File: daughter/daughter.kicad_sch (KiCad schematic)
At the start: 2 parts, among them U1 ESP32-C3, Y1 Crystal_GND24_Small

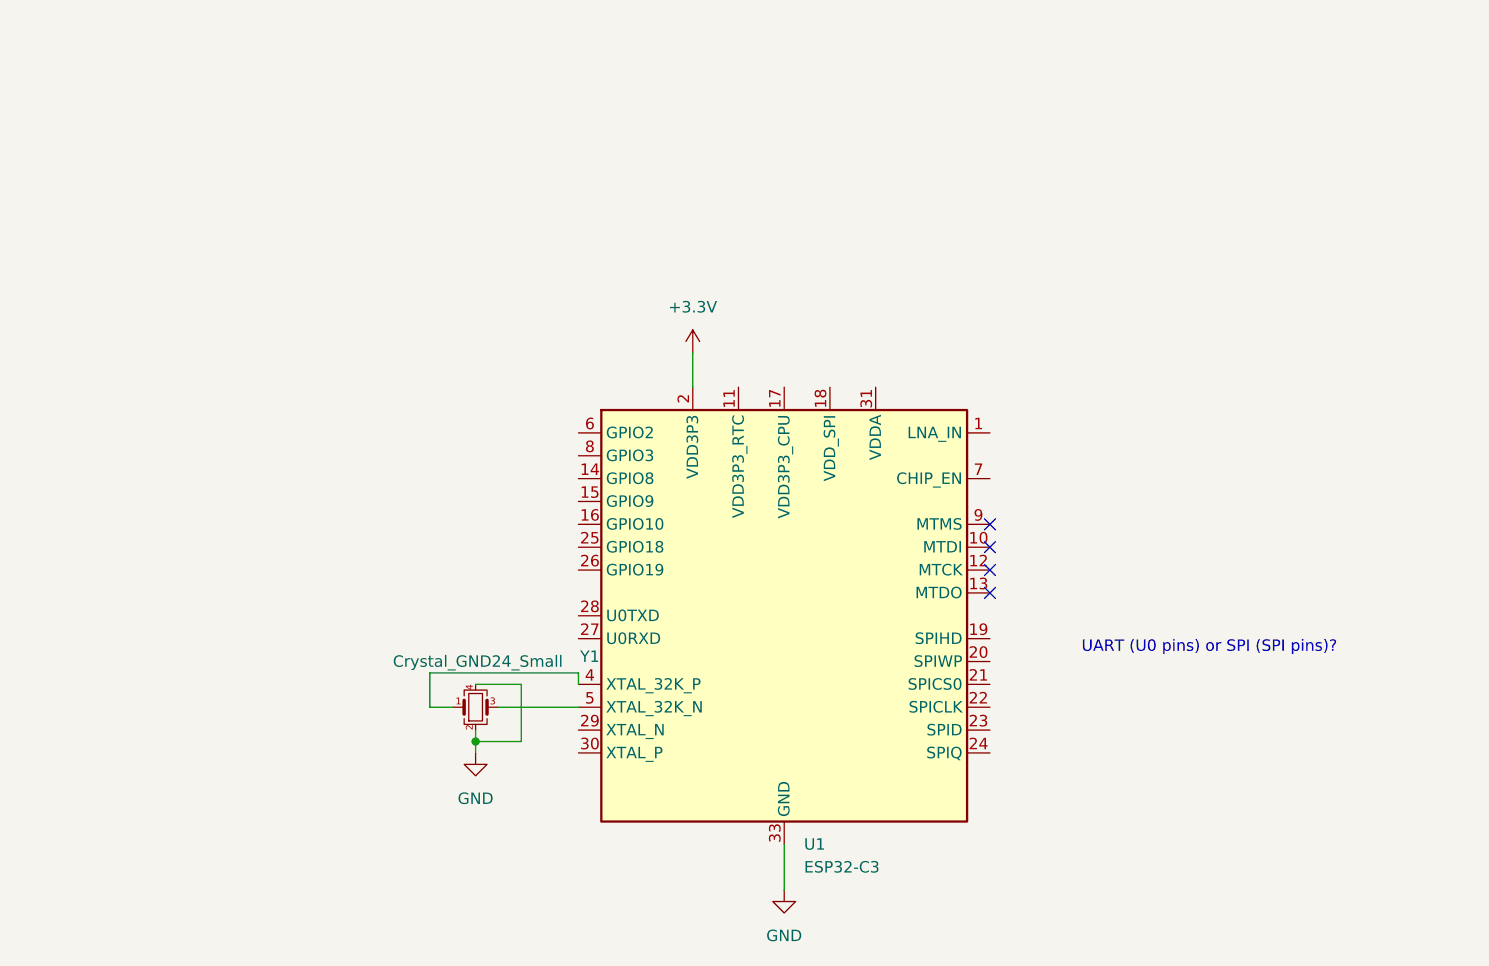
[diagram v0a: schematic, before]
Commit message: Daughterboard setup, labeling, and testpoints
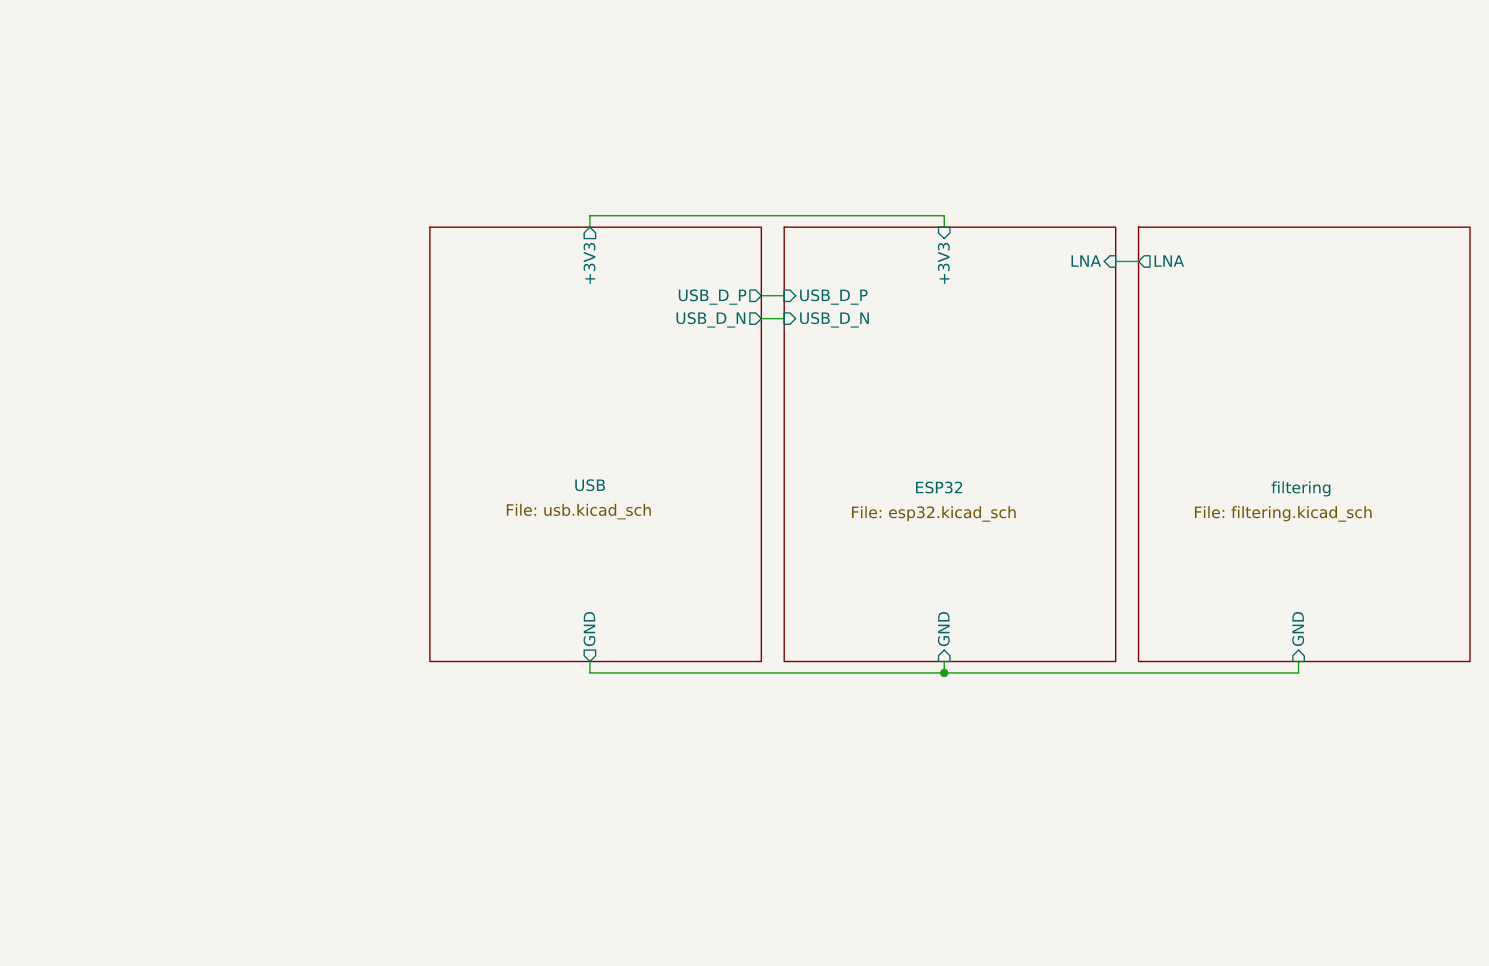
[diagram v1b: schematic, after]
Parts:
- removed U1: ESP32-C3, Package_DFN_QFN:QFN-32-1EP_5x5mm_P0.5mm_EP3.7x3.7mm, symbol MCU_Espressif:ESP32-C3
- removed Y1: Crystal_GND24_Small, symbol Device:Crystal_GND24_Small
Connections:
- no-connect marks 4 -> 0
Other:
- added sheet ESP32 (esp32.kicad_sch)
- added sheet USB (usb.kicad_sch)
- added sheet filtering (filtering.kicad_sch)
- note removed: "UART (U0 pins) or SPI (SPI pins)?"

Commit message: Common PSU
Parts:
- added J2: Screw_Terminal_01x03, TerminalBlock_TE-Connectivity:TerminalBlock_TE_282834-3_1x03_P2.54mm_Horizontal, symbol Connector:Screw_Terminal_01x03
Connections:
- new net Earth: J2.3 (Pin_3)
- new net LINE: J2.1 (Pin_1)
- new net NEUT: J2.2 (Pin_2)
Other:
- added sheet power (../power.kicad_sch)
- sheet USB ports: added +5V; removed none

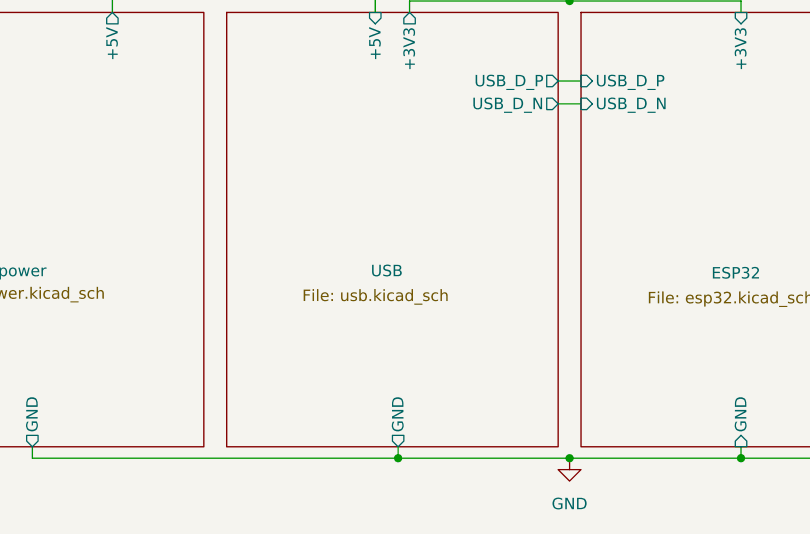
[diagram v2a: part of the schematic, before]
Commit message: Prep for more daughter IO
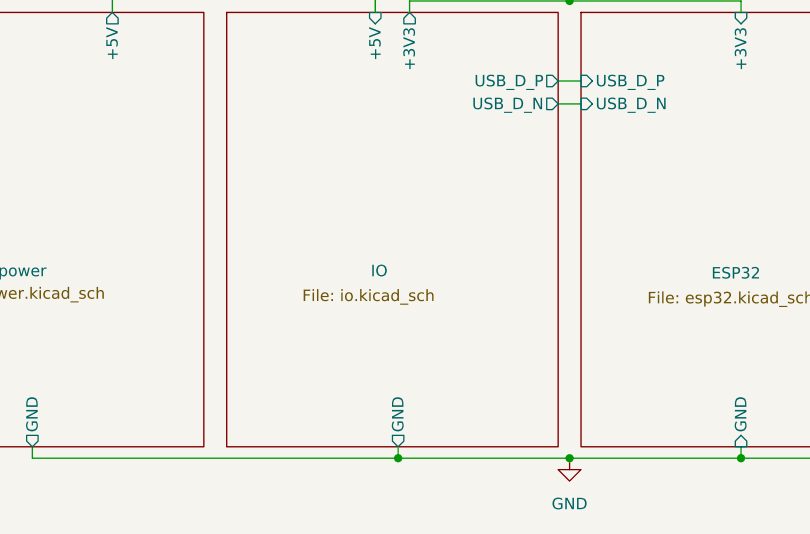
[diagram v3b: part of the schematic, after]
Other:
- sheet USB renamed IO
- sheet IO: file usb.kicad_sch -> io.kicad_sch
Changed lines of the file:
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@@
 			(color 0 0 0 0.0000)
 		)
-		(property "Sheetname" "USB"
+		(property "Sheetname" "IO"
 			(at 118.872 85.344 0)
 			(effects
@@
 			)
 		)
-		(property "Sheetfile" "usb.kicad_sch"
+		(property "Sheetfile" "io.kicad_sch"
 			(at 111.252 86.614 0)
 			(effects
